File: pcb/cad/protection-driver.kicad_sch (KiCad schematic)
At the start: 46 parts, among them J1 Vdc, J2 contactor, J4 PS1, K1 G5V-2, Q1 BC337, Q2 TIP122, SW1 SW_Push_Dual_x2, SW2 SW_Push_Dual_x2, SW3 SW_SPST, SW4 Protect_sel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

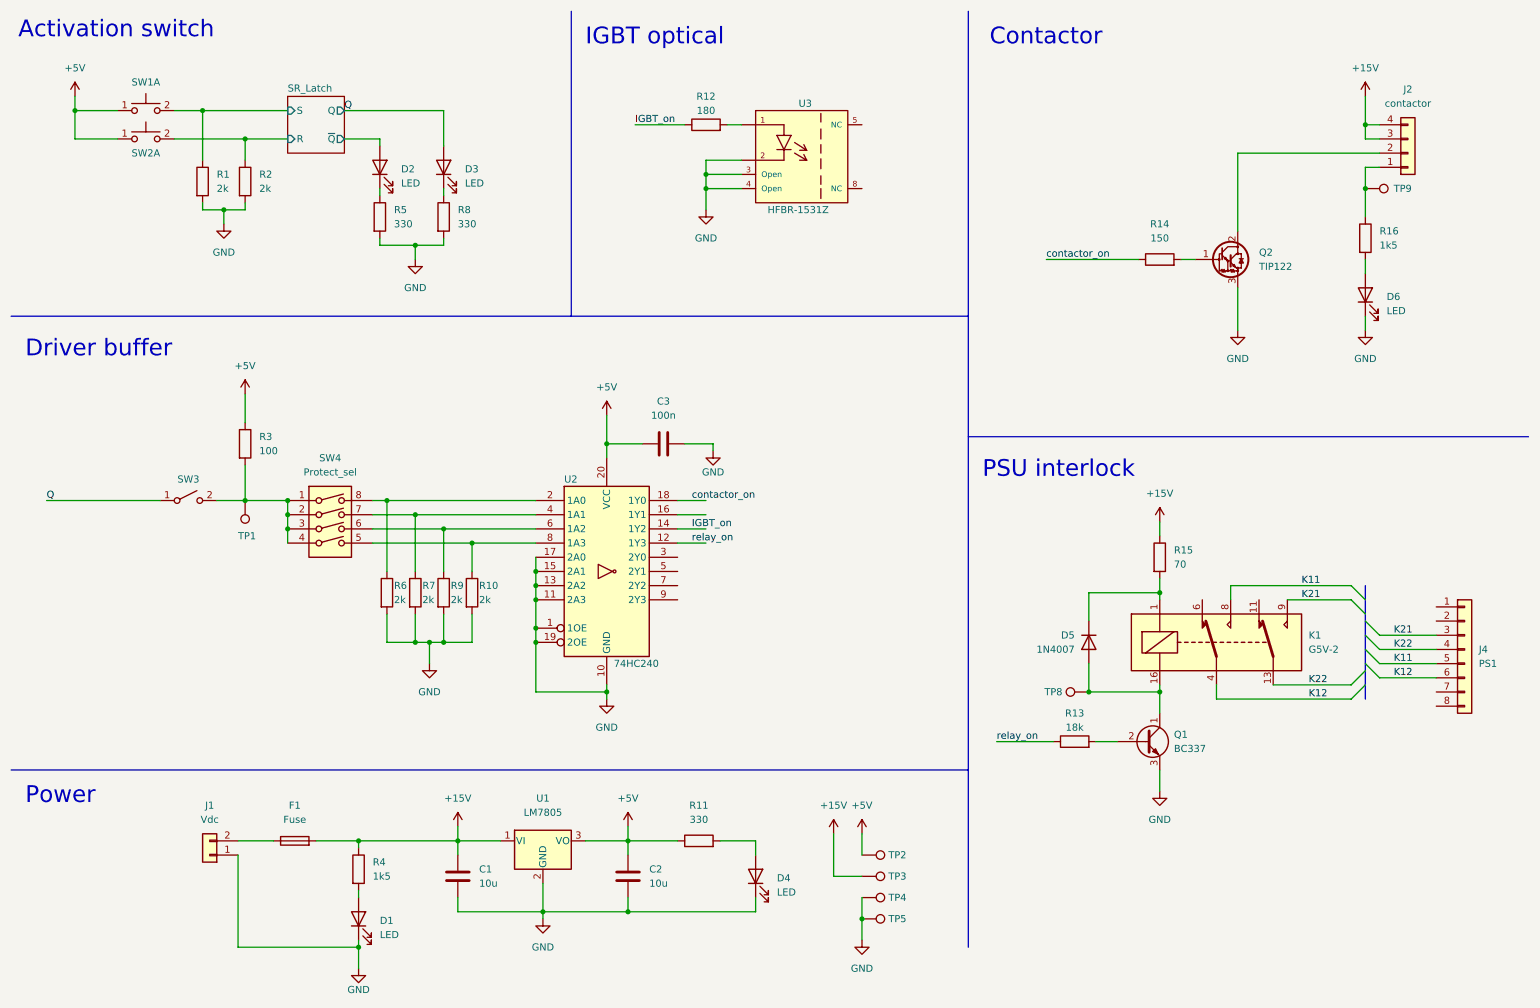
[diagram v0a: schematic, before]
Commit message: schematic formatting
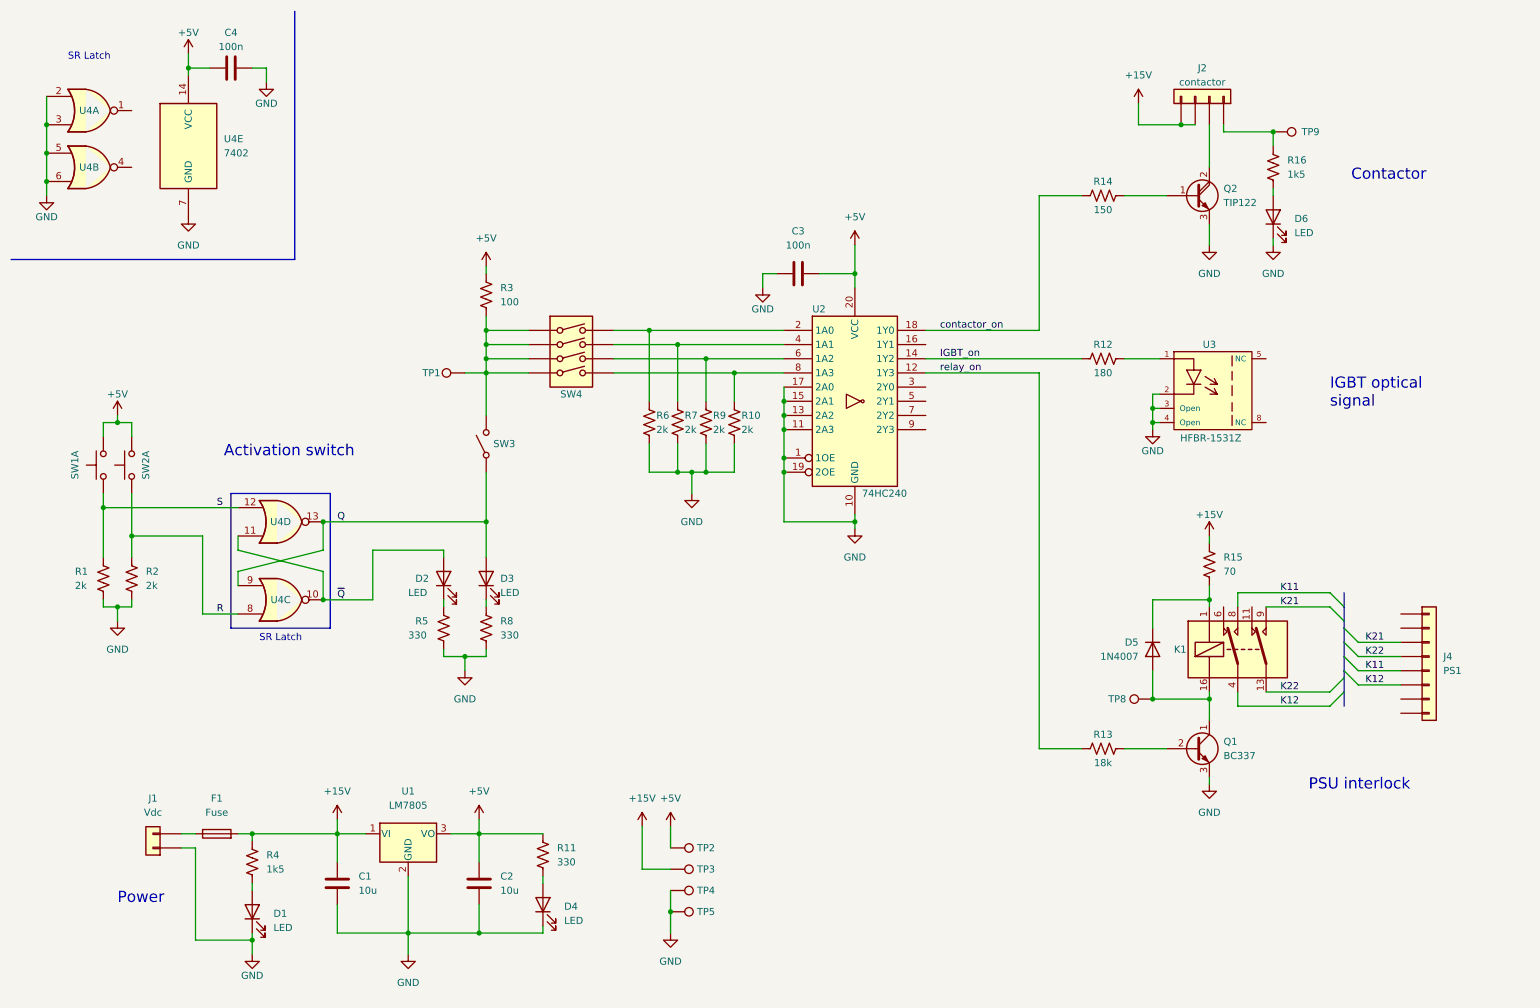
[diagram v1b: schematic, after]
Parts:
- removed K1: G5V-2, Relay_THT:Relay_DPDT_Omron_G5V-2, symbol Relay:G5V-2
- added C4: 100n, Capacitor_THT:C_Disc_D7.5mm_W5.0mm_P7.50mm, symbol Device:C
- added K1: ML2RC2, Relay_THT:Relay_DPDT_Omron_G5V-2, symbol Relay:Fujitsu_FTR-F1C
- added U4: 7402, Package_DIP:DIP-14_W7.62mm_Socket, symbol 74xx:7402
- Q2: symbol Transistor_BJT:TIP122 -> Device:Q_NPN_Darlington_BCE
- R1, R10, R11, R12, R13, R14, R15, R16, R2, R3, R4, R5, R6, R7, R8, R9: symbol Device:R -> Device:R_US
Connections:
- net +5V: now also C4.1, U4.14 (VCC)
- net GND: now also C4.2, U4.2, U4.3, U4.5, U4.6, U4.7 (GND)
- net K11: now also K1.8
- net K12: now also K1.4
- net K21: now also K1.9
- net K22: now also K1.13
- net Q: now also U4.13, U4.9
- net at D5.2 (A), Q1.1 (C), TP8.1: now also K1.16
- net at D5.1 (K), R15.2: now also K1.1
- net SR_Latch/R renamed R
- net R: now also U4.8
- net SR_Latch/S renamed S
- net S: now also U4.12
- net SR_Latch/~{Q} renamed ~{Q}
- net ~{Q}: now also U4.10, U4.11
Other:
- removed sheet SR_Latch
- note added: "IGBT optical signal"
- note added: "SR Latch"
- note removed: "Driver buffer"
- note removed: "IGBT optical"
- moved on the sheet: C1, C2, C3, D1, D2, D3, D4, D5, D6, F1, Q1, TP1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

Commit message: Include driver for second contactor with delayed activation
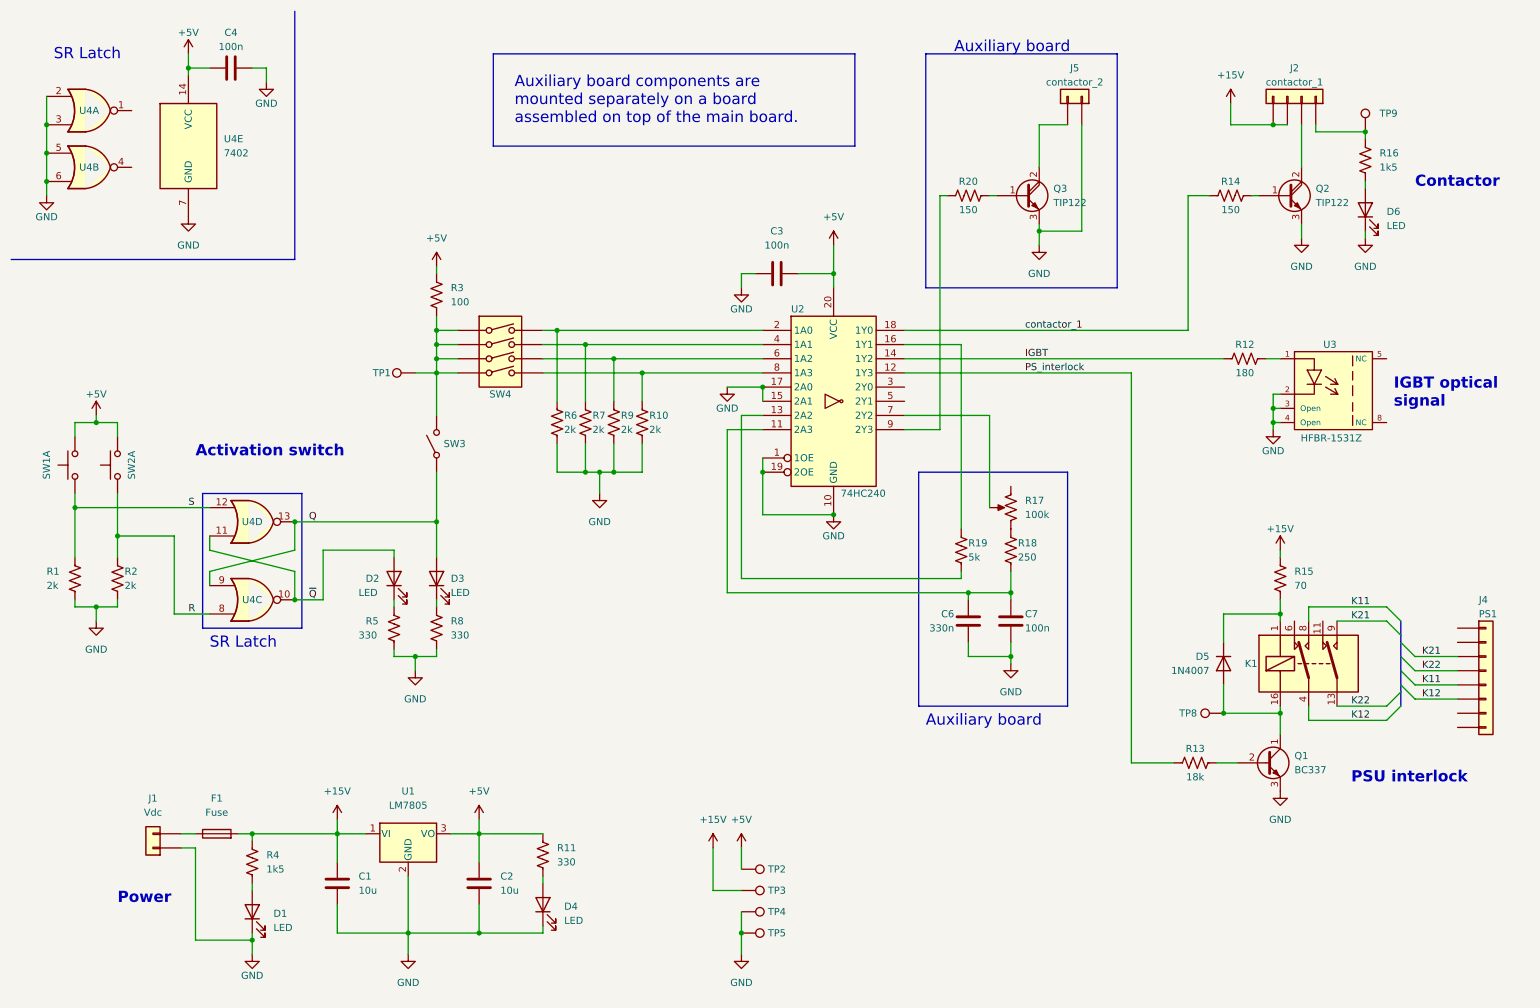
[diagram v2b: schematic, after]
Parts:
- added C6: 330n, symbol Device:C
- added C7: 100n, symbol Device:C
- added J5: contactor_2, symbol Connector_Generic:Conn_01x02
- added Q3: TIP122, Package_TO_SOT_THT:TO-220-3_Vertical, symbol Device:Q_NPN_Darlington_BCE
- added R17: 100k, symbol Device:R_Potentiometer_US
- added R18: 250, symbol Device:R_US
- added R19: 5k, symbol Device:R_US
- added R20: 150, Resistor_THT:R_Axial_DIN0207_L6.3mm_D2.5mm_P10.16mm_Horizontal, symbol Device:R_US
- J2: value contactor -> contactor_1
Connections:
- net GND: now also C6.2, C7.1, J5.1 (Pin_1), Q3.3 (E); no longer U2.11 (2A3), U2.13 (2A2)
- net at U2.16 (1Y1): now also R19.1
- net at U2.7 (2Y2): now also R17.2
- net at U2.9 (2Y3): now also R20.1
- net IGBT_on renamed IGBT
- net contactor_on renamed contactor_1
- net relay_on renamed PS_interlock
- new net: Q3.1 (B), R20.2
- new net: J5.2 (Pin_2), Q3.2 (C)
- new net: C6.1, C7.2, R18.2, U2.11 (2A3)
- new net: R19.2, U2.13 (2A2)
- new net: R17.3, R18.1
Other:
- note added: "Auxiliary board"
- note added: "Auxiliary board components are mounted separately on a board assembled on top of the main board."
- moved on the sheet: C3, D2, D3, D5, D6, J2, J4, K1, Q1, Q2, R1, R10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
